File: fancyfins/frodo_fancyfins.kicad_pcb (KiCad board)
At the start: 2 copper layers, 140 x 115 mm, 102 parts, among them J2 TC2050, U10 L78L05_SOT89, U11 L78L05_SOT89, U12 L78L05_SOT89, U13 L78L05_SOT89, U14 L78L05_SOT89, U15 L78L05_SOT89, U16 AZ1117-5.0, U17 W25Q128JVP, U18 L78L05_SOT89, U19 TPD4E1U06, U2 MCP2562-E-SN, U20 L78L05_SOT89, U3 AZ1117-3.3, U4 STM32F103RCTx, U7 L78L05_SOT89, U8 L78L05_SOT89, Y1 8MHz 12pF

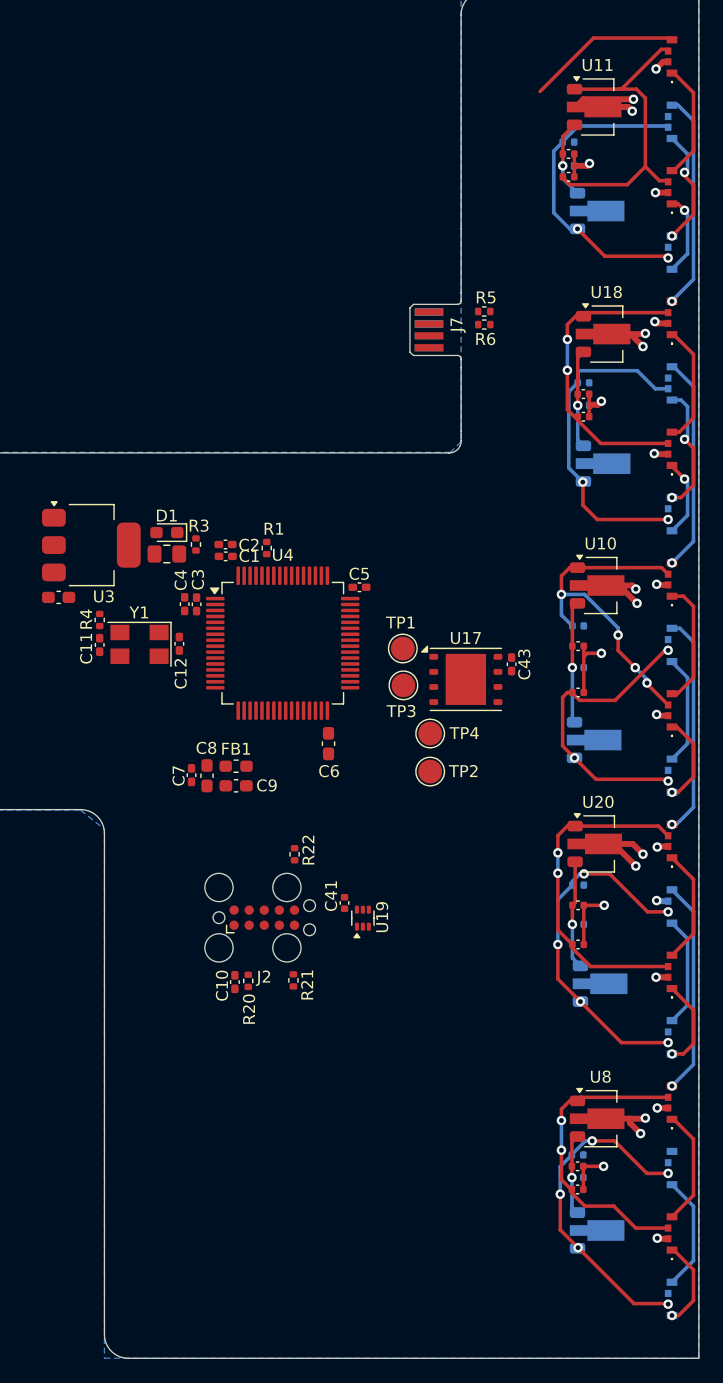
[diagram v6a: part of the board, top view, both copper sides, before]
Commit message: changed led routing
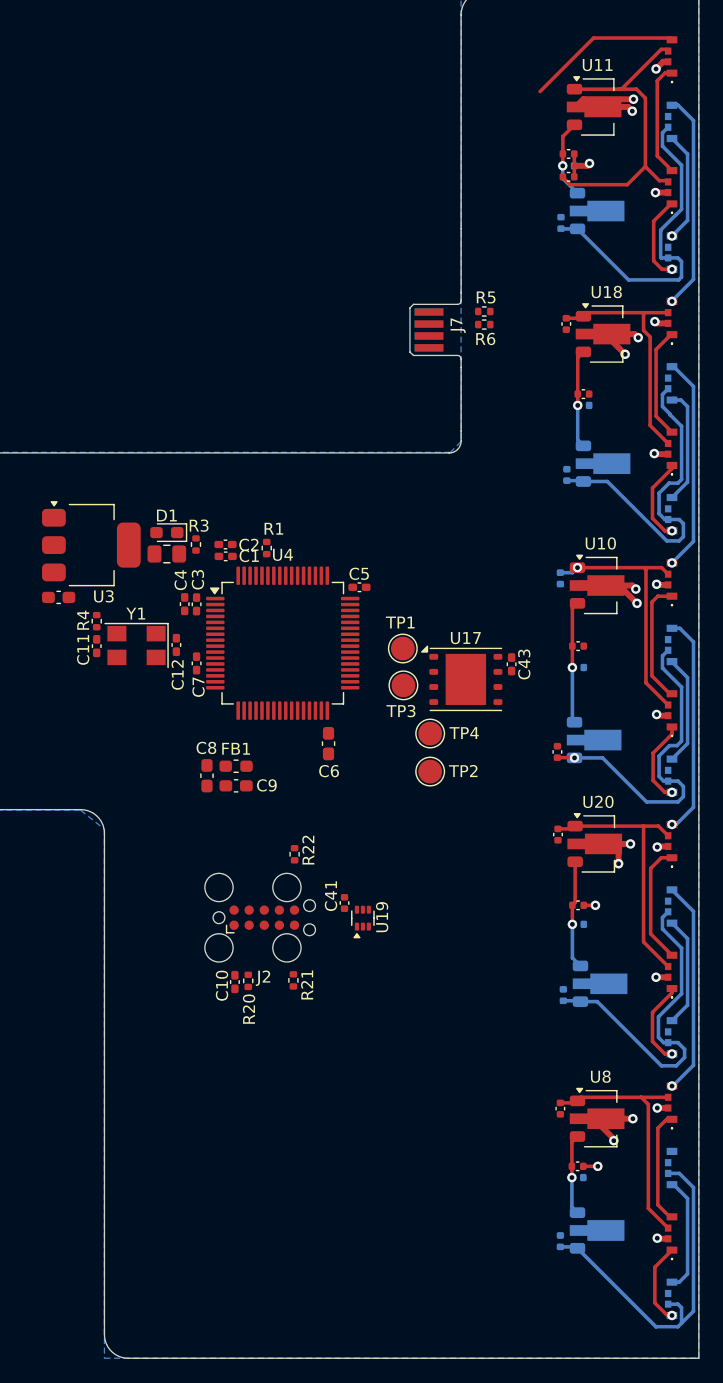
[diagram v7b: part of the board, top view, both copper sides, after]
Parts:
- moved C7 9.41 mm to (182.8, 91.5), turned to 90 degrees
- moved C45 9.40 mm to (213.2, 106.0), turned to -90 degrees
- moved C36 9.33 mm to (213.6, 119.5), turned to 90 degrees
- moved C38 7.93 mm to (213.8, 63.0), turned to -90 degrees
- moved C32 7.87 mm to (213.9, 75.7), turned to 90 degrees
- moved C30 7.39 mm to (213.3, 140.2), turned to 90 degrees
- moved C22 6.95 mm to (213.3, 129.0), turned to -90 degrees
- moved C20 6.83 mm to (213.4, 54.5), turned to 90 degrees
- moved C34 5.29 mm to (213.1, 99.0), turned to 90 degrees
- moved C26 4.27 mm to (213.3, 84.4), turned to -90 degrees
- moved C11 0.27 mm to (174.3, 90.1)
- moved C12 0.27 mm to (181.1, 90.0)
- moved R4 0.27 mm to (174.3, 88.0)
- moved Y1 0.27 mm to (177.7, 90.0)
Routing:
- net GND: track 86.0 -> 66.7 mm, vias 26 -> 23
- net Net-(D17-VDD): track 28.2 -> 21.9 mm, vias 4 -> 1
- net Net-(D30-VDD): track 28.6 -> 22.4 mm, vias 2 -> 0
- net Net-(D28-VDD): track 25.9 -> 20.6 mm, vias 2 -> 0
- net Net-(D15-VDD): track 26.2 -> 21.2 mm, vias 2 -> 0
- net Net-(D13-VDD): track 25.3 -> 28.2 mm, vias 3 -> 1
- net Net-(D19-VDD): track 28.3 -> 30.2 mm, vias 5 -> 0
- net Net-(D26-VDD): track 29.8 -> 28.3 mm, vias 5 -> 0
- net Net-(D10-DO): track 11.0 -> 9.93 mm, vias 2 -> 0
- net Net-(D18-DIN): track 10.9 -> 9.88 mm
- net Net-(D14-VDD): track 26.9 -> 27.8 mm, vias 2 -> 0
- net /LED_grouped6/DIN: track 6.58 -> 7.29 mm
- net Net-(D28-DO): track 10.1 -> 9.51 mm
- net Net-(D14-DIN): track 9.90 -> 9.29 mm, vias 2 -> 1
- net Net-(D30-DO): track 9.95 -> 10.5 mm
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
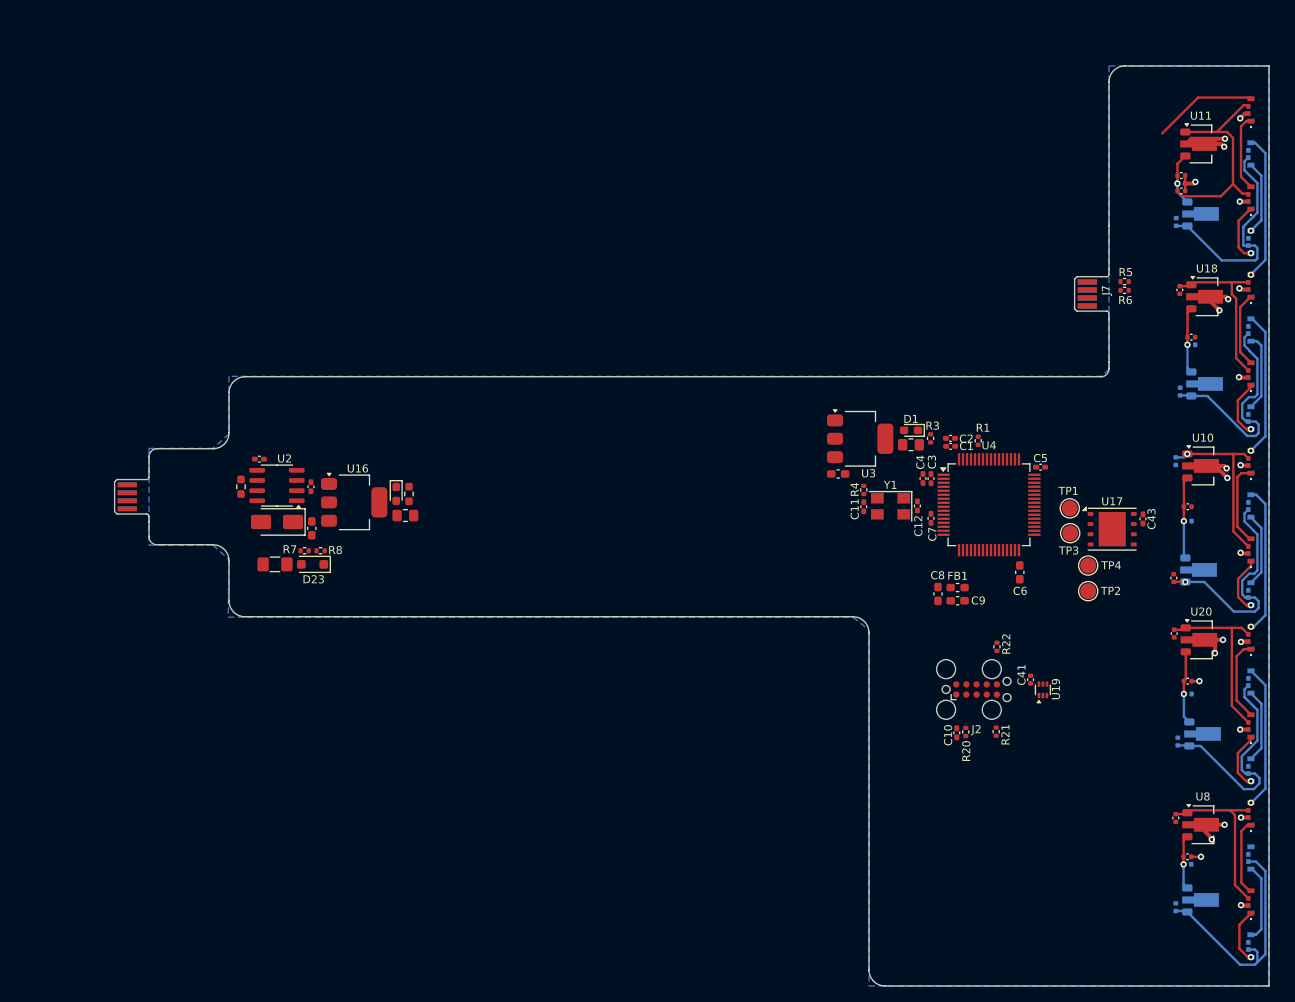
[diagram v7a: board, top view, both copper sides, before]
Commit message: changed led position
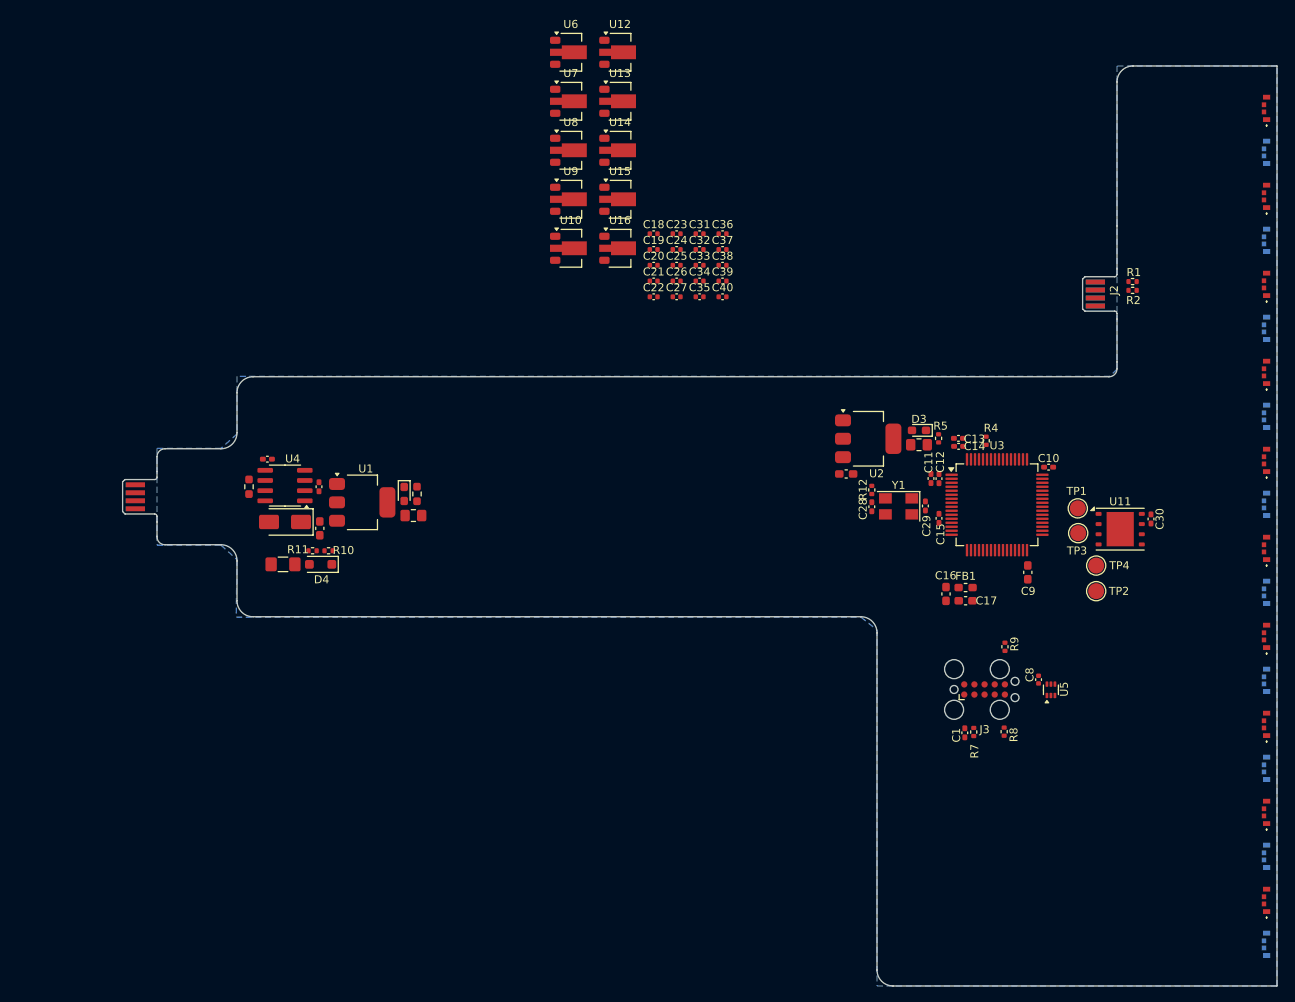
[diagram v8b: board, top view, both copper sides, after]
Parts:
- removed the C28 at (214.0, 50.6)
- removed the C29 at (214.8, 134.8)
- removed the C30 at (213.3, 140.2)
- removed C42: 330n, Capacitor_SMD:C_0402_1005Metric
- removed C45: 100n, Capacitor_SMD:C_0402_1005Metric
- removed D26, D27, D28, D29, D30, D31: 3210, fancyfins:1313210530000
- removed the D4 at (222.7, 57.0)
- removed the U11 at (216.5, 44.8)
- removed U18, U20: L78L05_SOT89, Package_TO_SOT_SMD:SOT-89-3
- added C18: 330n, Capacitor_SMD:C_0402_1005Metric, F.Cu at (148.1, 56.0)
- added C23: 100n, Capacitor_SMD:C_0402_1005Metric, F.Cu at (151.0, 56.0)
- added C24: 330n, Capacitor_SMD:C_0402_1005Metric, F.Cu at (151.0, 57.9)
- added C39: 330n, Capacitor_SMD:C_0402_1005Metric, F.Cu at (156.7, 61.9)
- added C40: 100n, Capacitor_SMD:C_0402_1005Metric, F.Cu at (156.7, 63.9)
- added D11: 3210, fancyfins:1313210530000, F.Cu at (224.7, 73.3)
- added D12: 3210, fancyfins:1313210530000, B.Cu at (224.7, 78.8)
- added D16: 3210, fancyfins:1313210530000, B.Cu at (224.7, 100.8)
- added D22: 3210, fancyfins:1313210530000, B.Cu at (224.7, 133.8)
- added D23: 3210, fancyfins:1313210530000, F.Cu at (224.7, 139.3)
- added D24: 3210, fancyfins:1313210530000, B.Cu at (224.7, 144.8)
- added D6: 3210, fancyfins:1313210530000, B.Cu at (224.7, 45.8)
- added U16: L78L05_SOT89, Package_TO_SOT_SMD:SOT-89-3, F.Cu at (143.9, 57.8)
- added U6: L78L05_SOT89, Package_TO_SOT_SMD:SOT-89-3, F.Cu at (137.7, 33.3)
- added U9: L78L05_SOT89, Package_TO_SOT_SMD:SOT-89-3, F.Cu at (137.7, 51.7)
- C19: value 330n -> 100n; moved to F.Cu
- C20, C26: value 100n -> 330n; moved to F.Cu
- C21, C25, C27: value 330n -> 100n
- C22: value 100n -> 330n
- C31, C32, C33, C35, C36, D13, D19, D21, D9, U12, U13, U14, U15, U7: moved to F.Cu
- D18, D8: moved to B.Cu
- moved U12 128.6 mm to (143.9, 33.3)
- moved U8 115.5 mm to (137.7, 45.5)
- moved U15 99.1 mm to (143.9, 51.7)
- moved C21 98.1 mm to (148.1, 61.9)
- moved C22 92.2 mm to (148.1, 63.9), turned to 0 degrees
- moved U14 89.6 mm to (143.9, 45.5)
- moved D5 88.2 mm to (224.7, 40.3)
- moved C36 85.2 mm to (156.7, 56.0), turned to 0 degrees
- moved U10 83.6 mm to (137.7, 57.8)
- moved D9 82.7 mm to (224.7, 62.3), turned to -90 degrees
- moved U13 81.4 mm to (143.9, 39.4)
- moved U7 80.3 mm to (137.7, 39.4)
- moved C35 78.7 mm to (153.8, 63.9)
- moved C25 70.7 mm to (151.0, 59.9)
- moved C34 69.9 mm to (153.8, 61.9), turned to 0 degrees
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- renumbered C10 to C1, C5 to C10, C4 to C11, C3 to C12, C2 to C13, C1 to C14, C7 to C15, C8 to C16, C9 to C17, C39 to C2, C11 to C28, C12 to C29, C40 to C3, C43 to C30, C49 to C4, C13 to C5, C14 to C6, C44 to C7, C41 to C8, C6 to C9, D25 to D1, D1 to D3, D23 to D4, J6 to J1, J7 to J2, J2 to J3, R5 to R1, R8 to R10, R7 to R11, R4 to R12, R6 to R2, R16 to R3, R1 to R4, R3 to R5, R2 to R6, R20 to R7, R21 to R8, R22 to R9, U16 to U1, U17 to U11, U3 to U2, U4 to U3, U2 to U4, U19 to U5
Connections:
- C19 pad 1: VD -> Net-(D5-VDD)
- C20 pad 1: Net-(D14-VDD) -> VD
- C21 pad 1: VD -> Net-(D7-VDD)
- C22 pad 1: Net-(D15-VDD) -> VD
- C25 pad 1: VD -> Net-(D11-VDD)
- C26 pad 1: Net-(D17-VDD) -> VD
- C27 pad 1: VD -> Net-(D13-VDD)
- C32 pad 1: Net-(D10-VDD) -> Net-(D15-VDD)
- C34 pad 1: Net-(D13-VDD) -> Net-(D17-VDD)
- C36 pad 1: Net-(D26-VDD) -> Net-(D19-VDD)
- C38 pad 1: Net-(D28-VDD) -> Net-(D21-VDD)
- D10 pad 4: /LED_grouped6/DIN -> Net-(D10-DIN)
- D13 pad 4: /LED_grouped3/DO -> Net-(D12-DO)
- D14 pad 1: /LED_grouped/DO -> LED_Signal_cont
- D14 pad 3: Net-(D14-VDD) -> Net-(D13-VDD)
- D14 pad 4: Net-(D14-DIN) -> Net-(D13-DO)
- D15 pad 1: /LED_grouped1/DO -> Net-(D15-DO)
- D15 pad 4: Net-(D15-DIN) -> LED_Signal_cont
- D17 pad 1: /LED_grouped3/DO -> Net-(D17-DO)
- D17 pad 4: Net-(D17-DIN) -> Net-(D16-DO)
- D18 pad 1: /LED_grouped/DIN -> Net-(D18-DO)
- D18 pad 3: Net-(D18-VDD) -> Net-(D17-VDD)
- D18 pad 4: Net-(D18-DIN) -> Net-(D17-DO)
- D19 pad 1: /LED_grouped5/DO -> Net-(D19-DO)
- D19 pad 4: Net-(D19-DIN) -> Net-(D18-DO)
- D20 pad 1: /LED_grouped3/DIN -> Net-(D20-DO)
- D20 pad 3: Net-(D10-VDD) -> Net-(D19-VDD)
- D20 pad 4: Net-(D10-DO) -> Net-(D19-DO)
- D21 pad 1: /LED_grouped2/DIN -> Net-(D21-DO)
- D21 pad 3: Net-(D13-VDD) -> Net-(D21-VDD)
- D21 pad 4: Net-(D13-DO) -> Net-(D20-DO)
- D5 pad 1: Net-(D15-DIN) -> Net-(D5-DO)
- D5 pad 3: Net-(D15-VDD) -> Net-(D5-VDD)
- D5 pad 4: /LED_grouped1/DIN -> LED_Signal
- D7 pad 1: Net-(D17-DIN) -> Net-(D7-DO)
- D7 pad 3: Net-(D17-VDD) -> Net-(D7-VDD)
- D7 pad 4: /LED_grouped3/DIN -> Net-(D6-DO)
- D8 pad 1: Net-(D18-DIN) -> Net-(D8-DO)
- D8 pad 3: Net-(D18-VDD) -> Net-(D7-VDD)
- D8 pad 4: LED_Signal -> Net-(D7-DO)
- D9 pad 1: Net-(D19-DIN) -> Net-(D10-DIN)
- D9 pad 3: Net-(D19-VDD) -> Net-(D10-VDD)
- D9 pad 4: /LED_grouped1/DO -> Net-(D8-DO)
- U10 pad 1: Net-(D17-VDD) -> Net-(D13-VDD)
- U12 pad 1: Net-(D19-VDD) -> Net-(D15-VDD)
- U13 pad 1: Net-(D10-VDD) -> Net-(D17-VDD)
- U14 pad 1: Net-(D13-VDD) -> Net-(D19-VDD)
- U15 pad 1: Net-(D26-VDD) -> Net-(D21-VDD)
- U7 pad 1: Net-(D14-VDD) -> Net-(D7-VDD)
- U8 pad 1: Net-(D15-VDD) -> Net-(D10-VDD)
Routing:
- net GND: track 66.7 -> 0.00 mm, vias 23 -> 0
- net VD: track 41.4 -> 0.00 mm, vias 5 -> 0
- net Net-(D19-VDD): track 30.2 -> 0.00 mm
- net Net-(D26-VDD): track 28.3 -> 0.00 mm
- net Net-(D10-VDD): track 28.3 -> 0.00 mm
- net Net-(D13-VDD): track 28.2 -> 0.00 mm, vias 1 -> 0
- net Net-(D14-VDD): track 27.8 -> 0.00 mm
- net Net-(D18-VDD): track 27.6 -> 0.00 mm
- net Net-(D30-VDD): track 22.4 -> 0.00 mm
- net Net-(D17-VDD): track 21.9 -> 0.00 mm, vias 1 -> 0
- net Net-(D15-VDD): track 21.2 -> 0.00 mm
- net Net-(D28-VDD): track 20.6 -> 0.00 mm
- net /LED_grouped2/DIN: track 18.6 -> 0.00 mm, vias 1 -> 0
- net /LED_grouped/DO: track 18.3 -> 0.00 mm, vias 1 -> 0
- net /LED_grouped3/DIN: track 18.1 -> 0.00 mm, vias 1 -> 0
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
